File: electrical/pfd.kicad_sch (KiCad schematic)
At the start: 8 parts

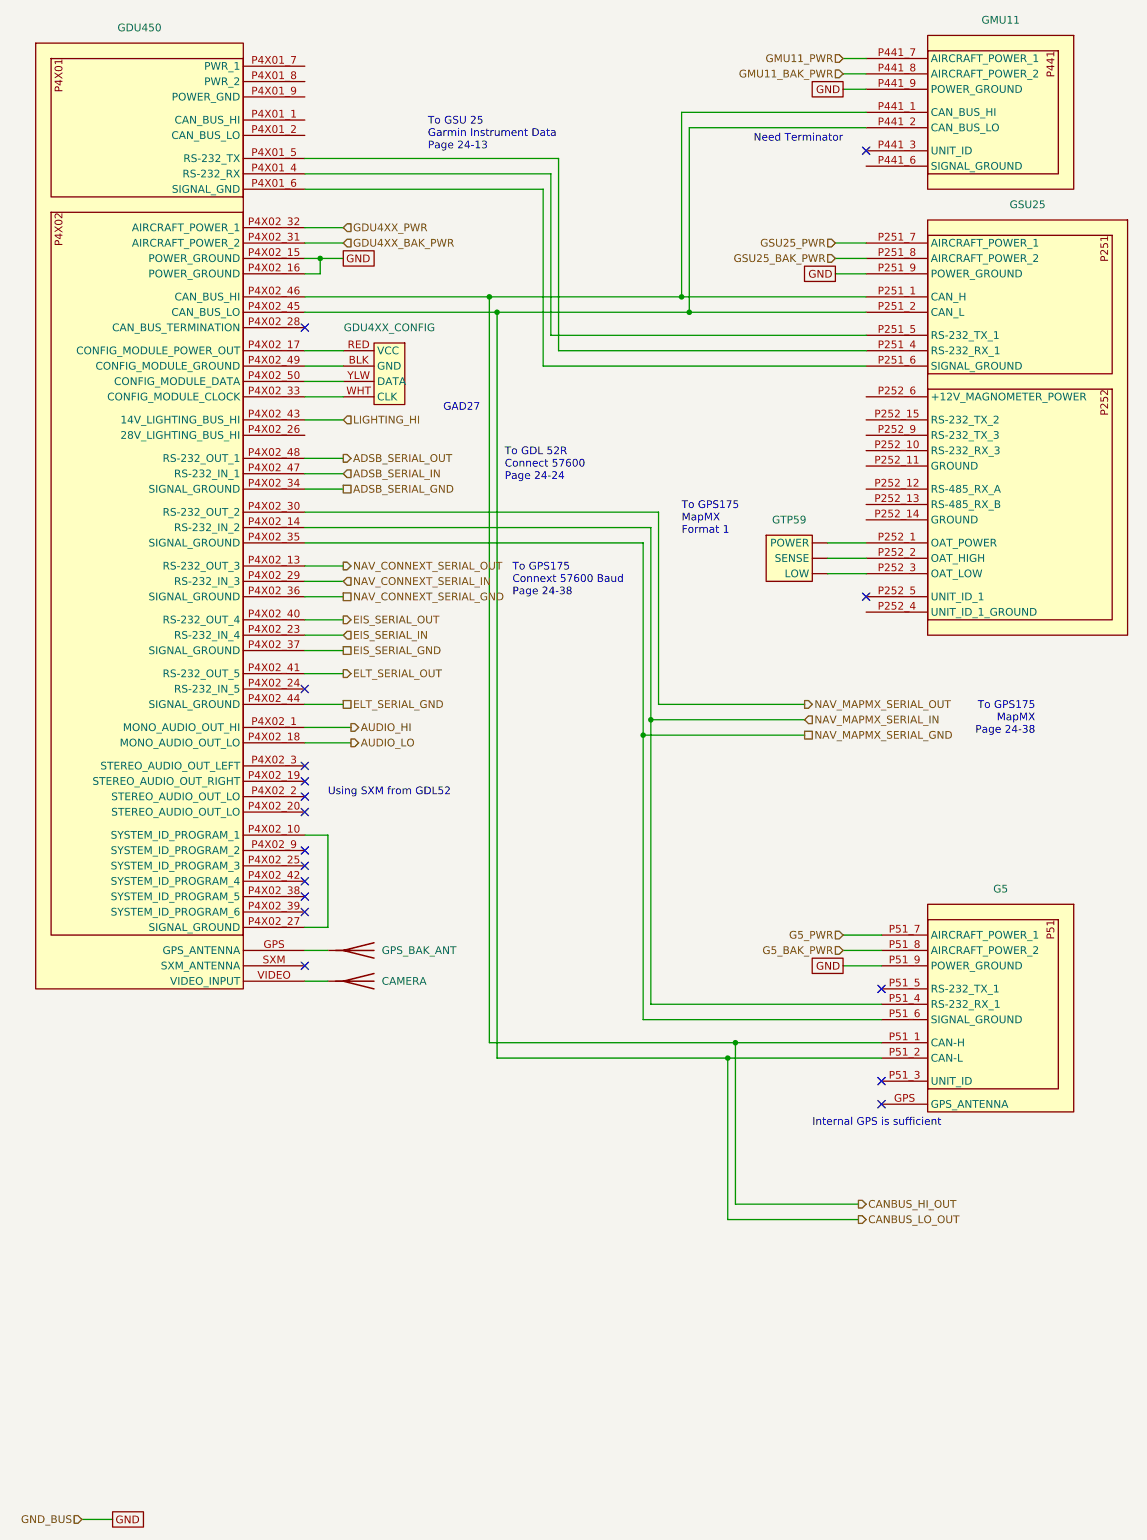
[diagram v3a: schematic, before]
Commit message: Updated electrical to not use IBBS. Also, added BT adapter and 3P3T switch.
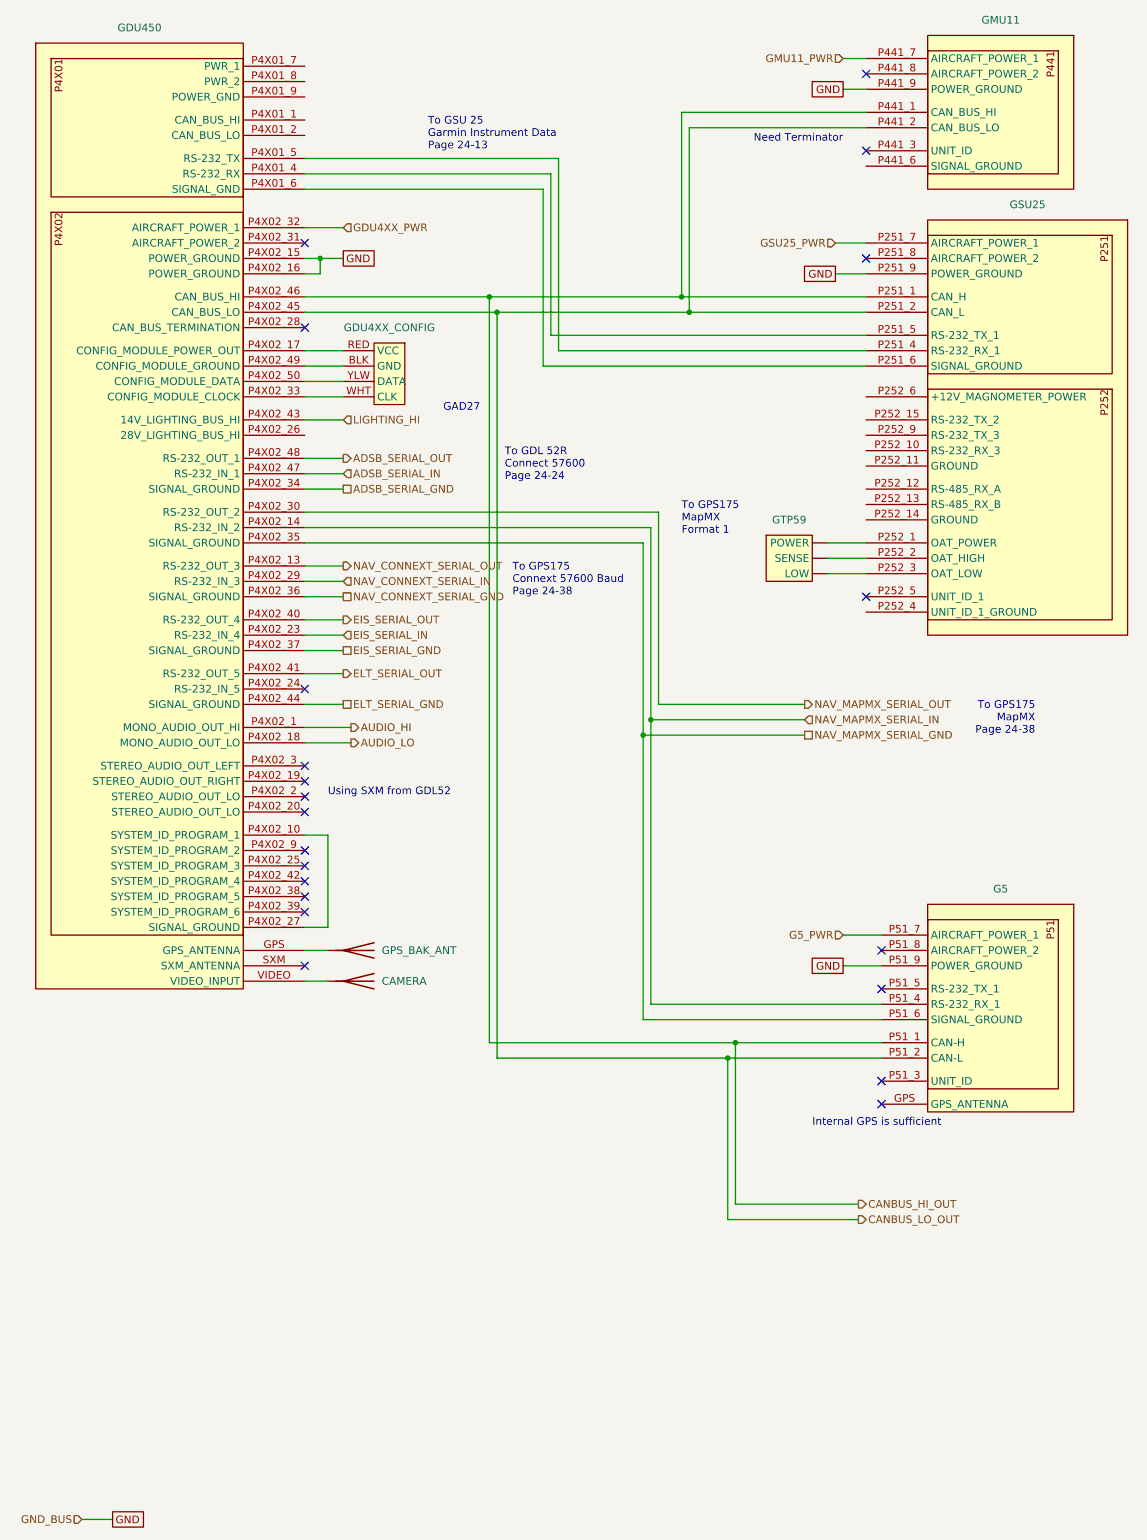
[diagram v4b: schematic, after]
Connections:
- net G5_BAK_PWR: no longer names the net of G5.P51_8 (AIRCRAFT_POWER_2)
- net GDU4XX_BAK_PWR: no longer names the net of GDU450.P4X02_31 (AIRCRAFT_POWER_2)
- net GMU11_BAK_PWR: no longer names the net of GMU11.P441_8 (AIRCRAFT_POWER_2)
- net GSU25_BAK_PWR: no longer names the net of GSU25.P251_8 (AIRCRAFT_POWER_2)
- no-connect marks 17 -> 21
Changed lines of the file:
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@@
   (junction (at 64.77 53.34) (diameter 0) (color 0 0 0 0)
   )
+  (no_connect (at 154.94 22.86))
   (no_connect (at 157.48 193.04))
   (no_connect (at 62.23 151.13))
   (no_connect (at 154.94 35.56))
   (no_connect (at 62.23 156.21))
+  (no_connect (at 154.94 53.34))
   (no_connect (at 157.48 189.23))
   (no_connect (at 62.23 161.29))
   (no_connect (at 62.23 144.78))
   (no_connect (at 62.23 124.46))
+  (no_connect (at 157.48 167.64))
   (no_connect (at 154.94 109.22))
   (no_connect (at 62.23 153.67))
@@
   (no_connect (at 62.23 137.16))
   (no_connect (at 62.23 142.24))
+  (no_connect (at 62.23 50.8))
   (wire (pts (xy 154.94 68.58) (xy 104.14 68.58))
     (stroke (width 0) (type default))
@@
     (stroke (width 0) (type default))
   )
-  (wire (pts (xy 151.13 22.86) (xy 154.94 22.86))
-    (stroke (width 0) (type default))
-  )
   (wire (pts (xy 62.23 80.01) (xy 68.58 80.01))
     (stroke (width 0) (type default))
@@
     (stroke (width 0) (type default))
   )
-  (wire (pts (xy 149.86 53.34) (xy 154.94 53.34))
-    (stroke (width 0) (type default))
-  )
   (wire (pts (xy 62.23 62.23) (xy 93.98 62.23))
     (stroke (width 0) (type default))
@@
     (stroke (width 0) (type default))
   )
-  (wire (pts (xy 62.23 50.8) (xy 68.58 50.8))
-    (stroke (width 0) (type default))
-  )
   (wire (pts (xy 120.65 127) (xy 144.78 127))
     (stroke (width 0) (type default))
@@
   )
   (wire (pts (xy 62.23 73.66) (xy 68.58 73.66))
-    (stroke (width 0) (type default))
-  )
-  (wire (pts (xy 151.13 167.64) (xy 157.48 167.64))
     (stroke (width 0) (type default))
   )
@@
     (effects (font (size 1.27 1.27)) (justify left))
   )
-  (hierarchical_label "GMU11_BAK_PWR" (shape input) (at 151.13 22.86 180) (fields_autoplaced)
-    (effects (font (size 1.27 1.27)) (justify right))
-  )
   (hierarchical_label "LIGHTING_HI" (shape input) (at 68.58 80.01 0) (fields_autoplaced)
     (effects (font (size 1.27 1.27)) (justify left))
@@
     (effects (font (size 1.27 1.27)) (justify left))
   )
-  (hierarchical_label "GDU4XX_BAK_PWR" (shape input) (at 68.58 50.8 0) (fields_autoplaced)
-    (effects (font (size 1.27 1.27)) (justify left))
-  )
   (hierarchical_label "ELT_SERIAL_OUT" (shape output) (at 68.58 121.92 0) (fields_autoplaced)
     (effects (font (size 1.27 1.27)) (justify left))
@@
     (effects (font (size 1.27 1.27)) (justify right))
   )
-  (hierarchical_label "GSU25_BAK_PWR" (shape input) (at 149.86 53.34 180) (fields_autoplaced)
-    (effects (font (size 1.27 1.27)) (justify right))
-  )
   (hierarchical_label "NAV_CONNEXT_SERIAL_GND" (shape passive) (at 68.58 109.22 0) (fields_autoplaced)
     (effects (font (size 1.27 1.27)) (justify left))
@@
     (effects (font (size 1.27 1.27)) (justify left))
   )
-  (hierarchical_label "G5_BAK_PWR" (shape input) (at 151.13 167.64 180) (fields_autoplaced)
-    (effects (font (size 1.27 1.27)) (justify right))
-  )
   (symbol (lib_id "flyerx:Garmin_GTP59") (at 138.43 99.06 0) (unit 1)

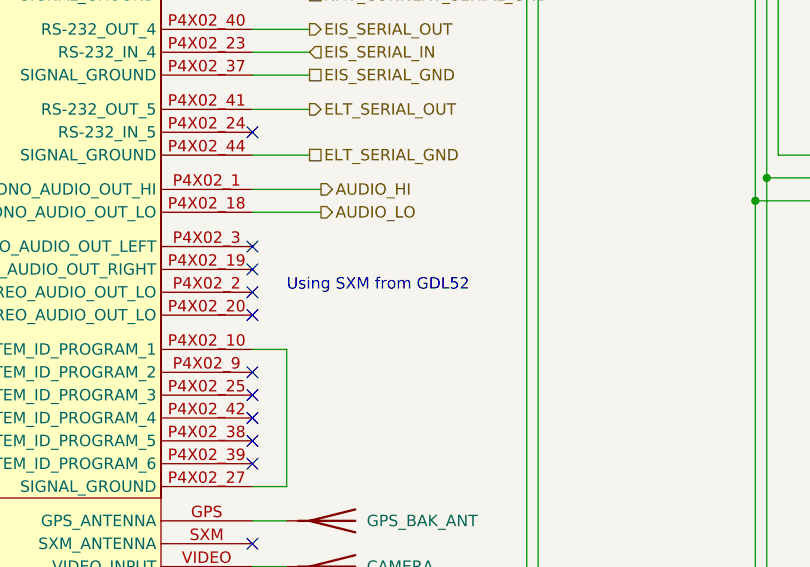
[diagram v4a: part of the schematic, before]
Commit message: Changed to have ELT with GPS. Also, changed Flaps to have position sensor. Added in wiring for all the sensors.
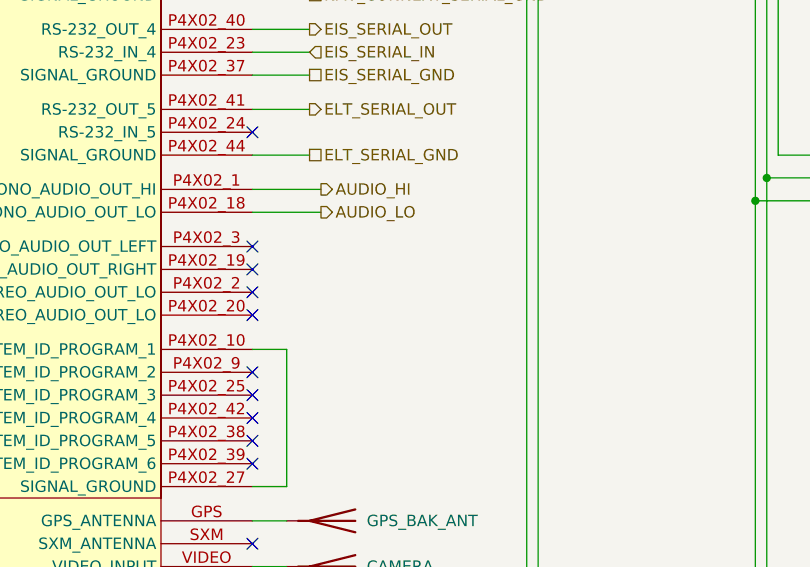
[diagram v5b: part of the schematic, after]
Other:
- note removed: "Using SXM from GDL52"
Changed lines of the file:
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@@
     (stroke (width 0) (type default))
-  )
-  (text "Using SXM from GDL52" (at 66.04 142.24 0)
-    (effects (font (size 1.27 1.27)) (justify left bottom))
   )
   (text "GAD27" (at 85.09 78.74 0)

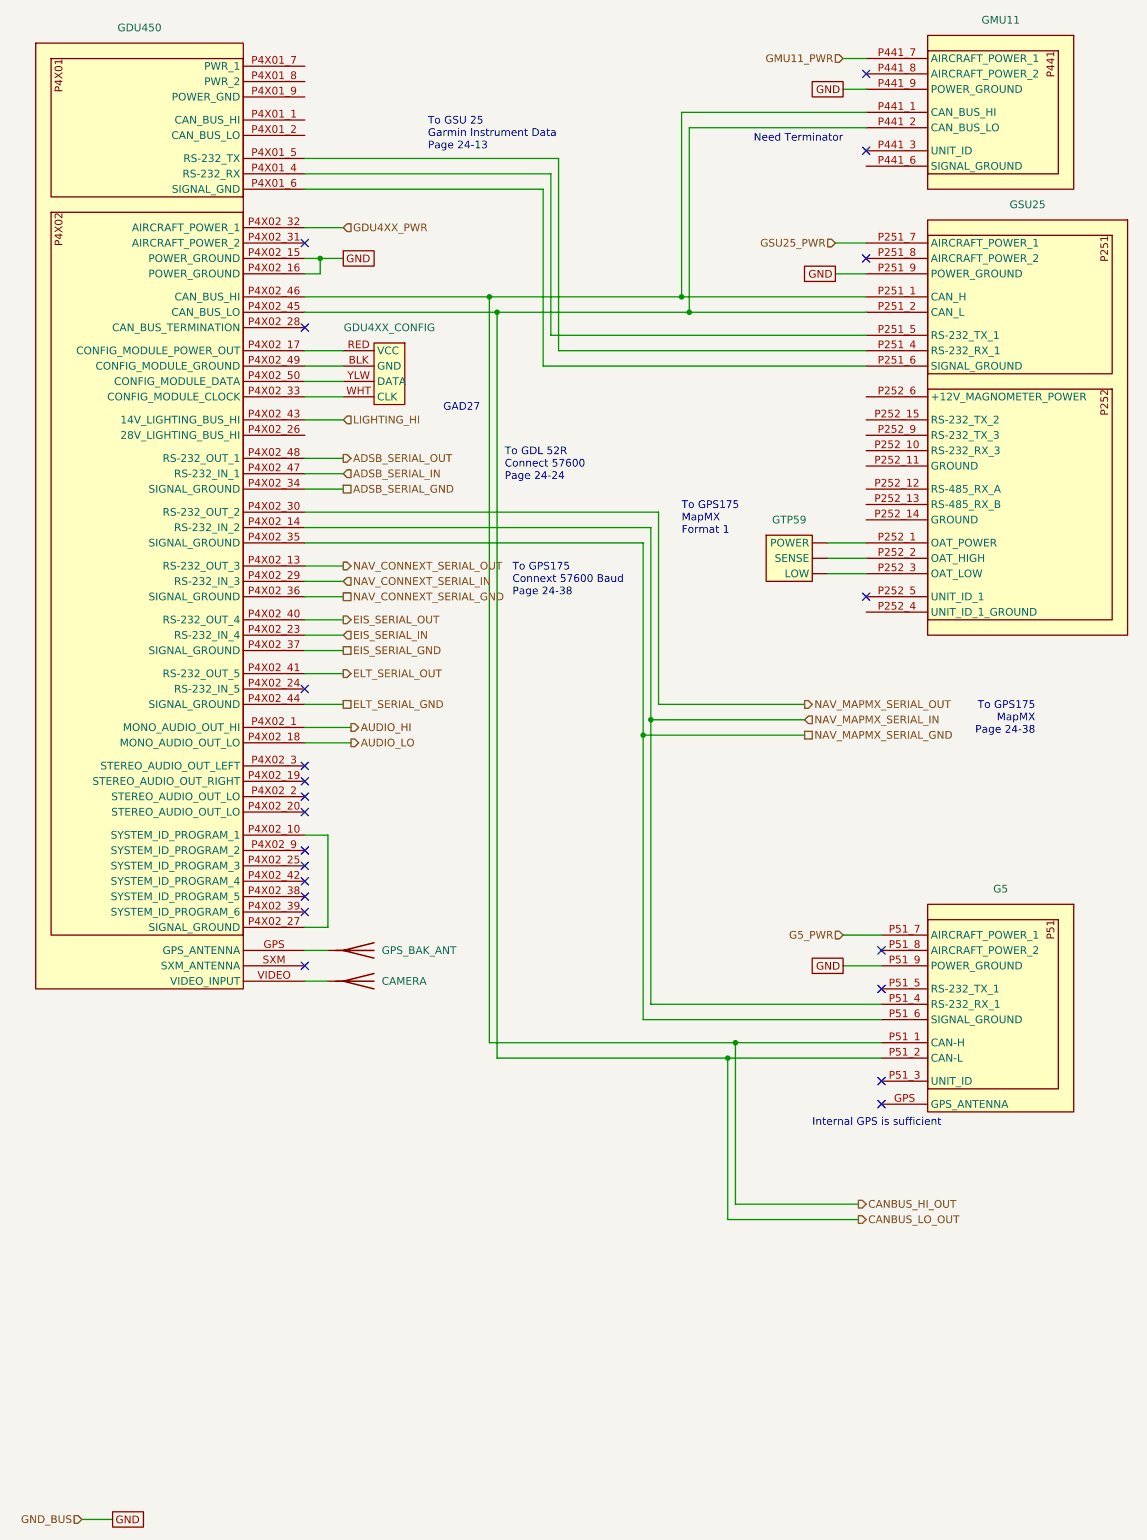
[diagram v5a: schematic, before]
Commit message: Updated canbus diagrams with order for where magnometer and servos will be located. Added yaw servo.
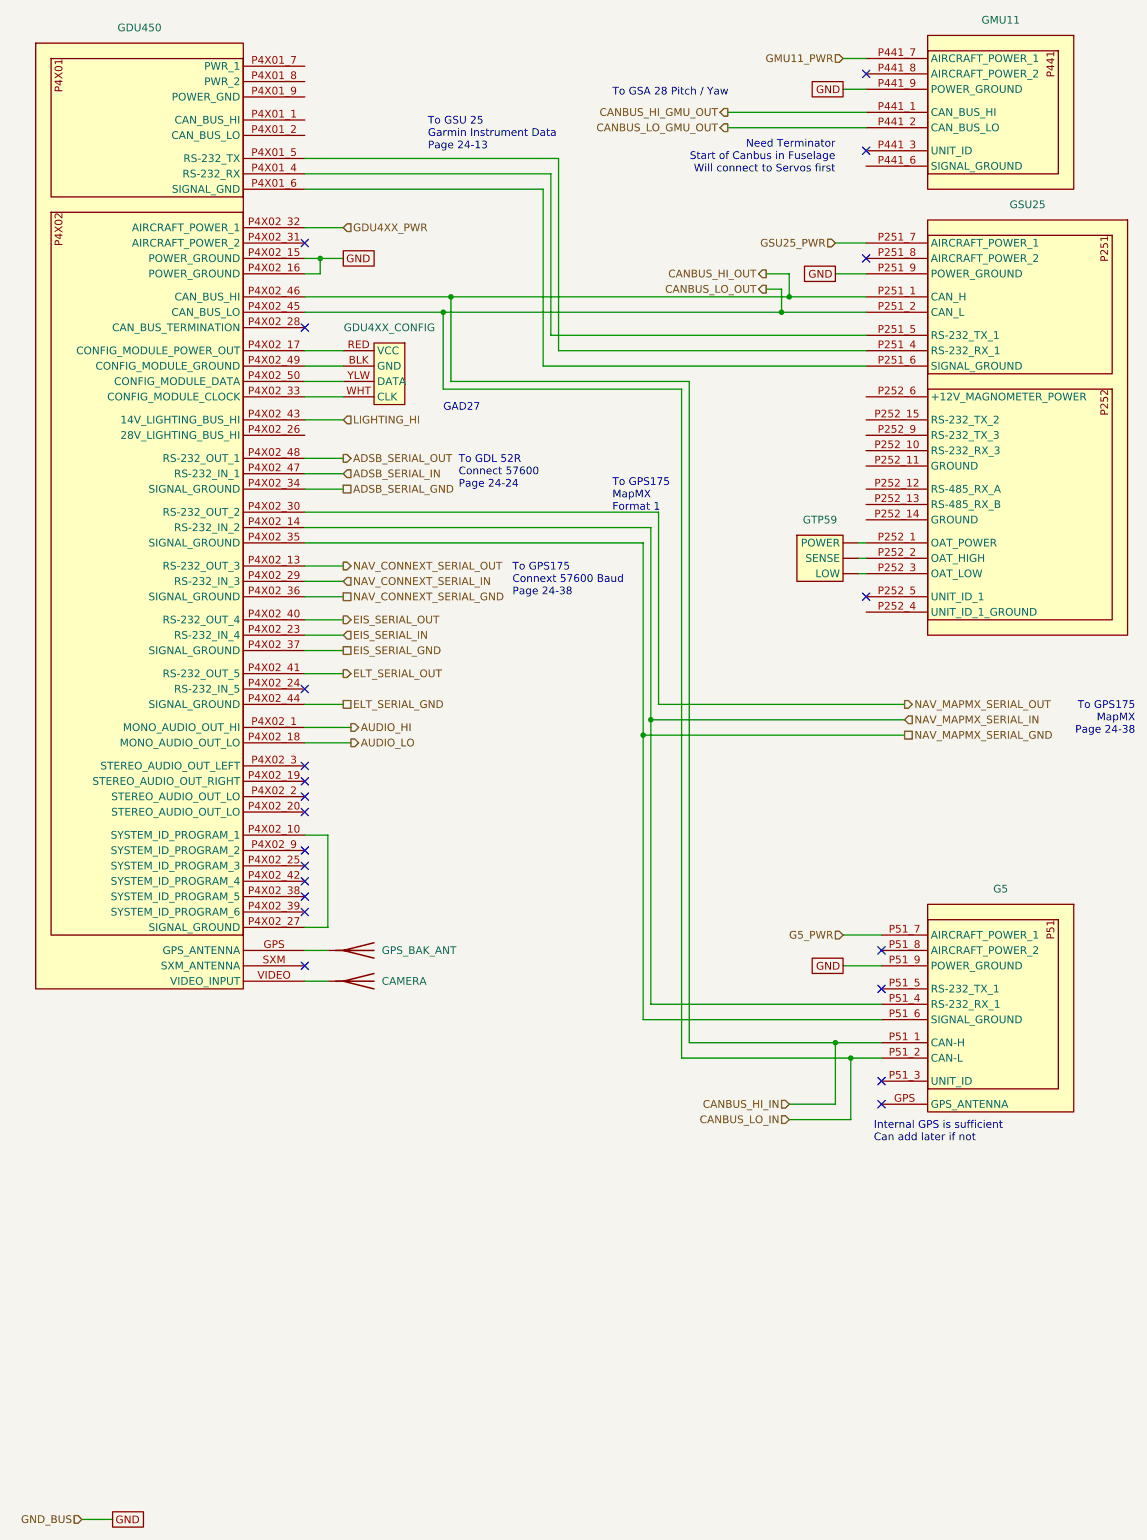
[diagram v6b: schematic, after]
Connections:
- net CANBUS_HI_OUT renamed CANBUS_HI_IN
- net CANBUS_HI_IN: no longer GMU11.P441_1 (CAN_BUS_HI)
- net CANBUS_LO_OUT renamed CANBUS_LO_IN
- net CANBUS_LO_IN: no longer GMU11.P441_2 (CAN_BUS_LO)
- new net CANBUS_HI_GMU_OUT: GMU11.P441_1 (CAN_BUS_HI)
- new net CANBUS_LO_GMU_OUT: GMU11.P441_2 (CAN_BUS_LO)
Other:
- note added: "Internal GPS is sufficient Can add later if not"
- note added: "Need Terminator Start of Canbus in Fuselage Will connect to Servos first"
- note added: "To GSA 28 Pitch / Yaw"
- note removed: "Internal GPS is sufficient"
- note removed: "Need Terminator"
- moved on the sheet: GTP59
